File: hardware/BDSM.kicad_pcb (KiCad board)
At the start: 2 copper layers, 80 x 56 mm, 97 parts, among them J1 614105150721, Q1 BC847, Q2 BC847, Q3 BSS138, Q4 BSS138, Q5 BSS138, SW1 "ON/OFF", U1 MAX16054AZT+T, U2 BQ24070, U3 TPS63001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

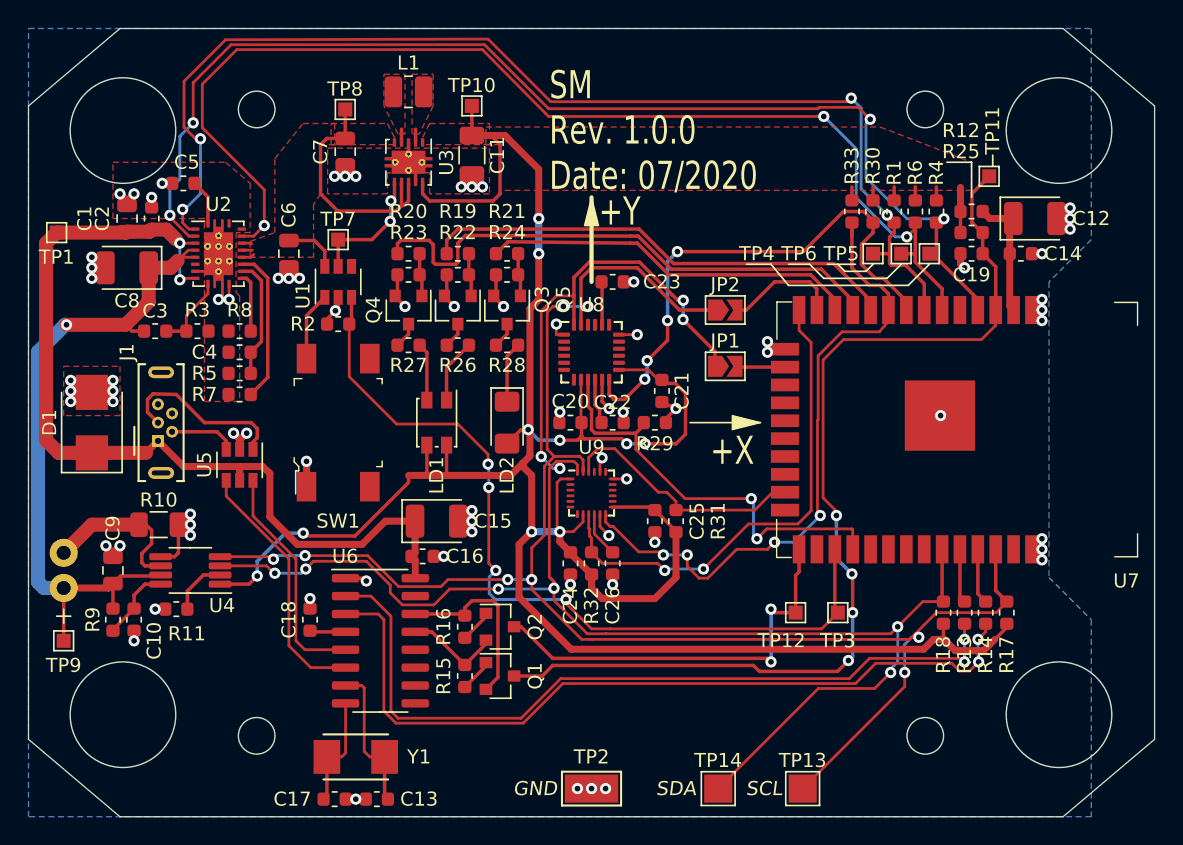
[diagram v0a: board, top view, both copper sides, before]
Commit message: Fix ESP32 powering errors
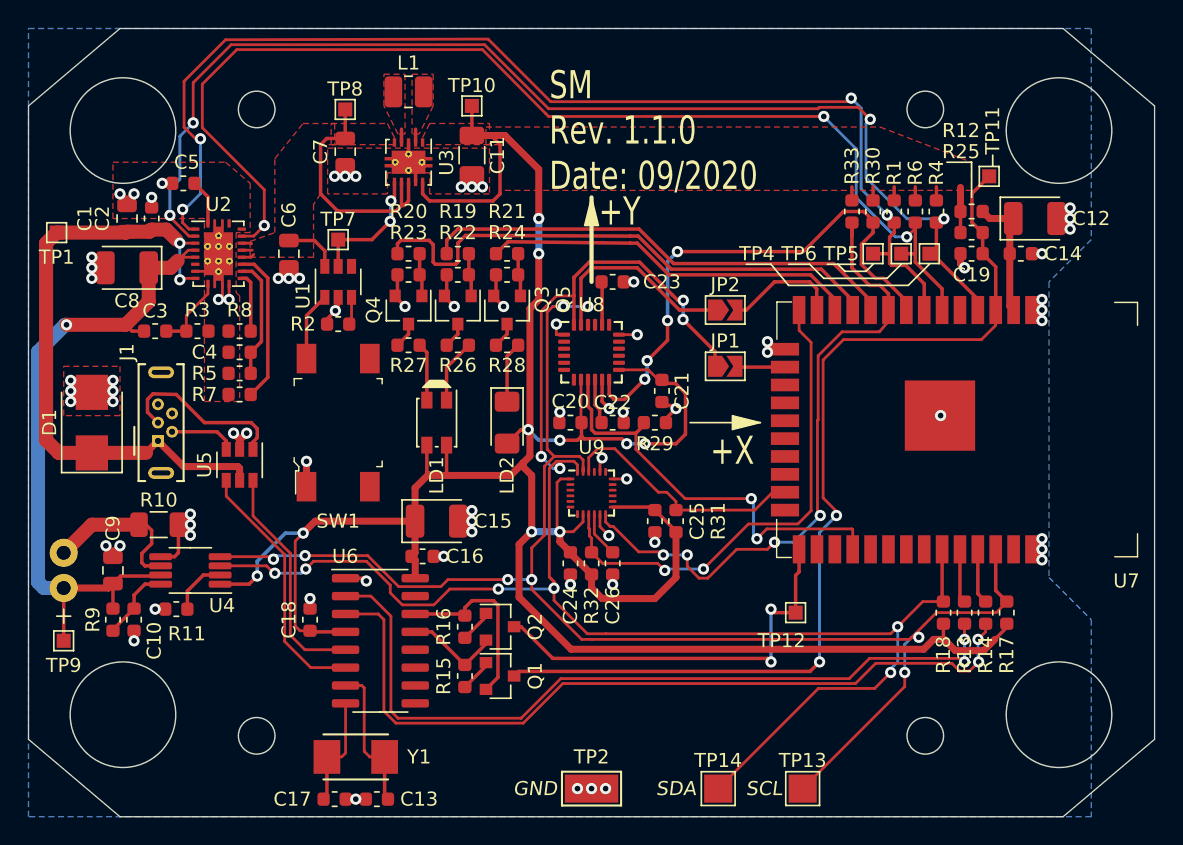
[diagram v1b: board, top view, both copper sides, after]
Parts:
- removed TP3: MCU-PWR, TestPoint:TestPoint_Pad_1.0x1.0mm
- Q1, Q2: value BC847 -> SS8050
- R32: value 10k -> DNP
- U9: value MPU-9250 -> DNP (MPU-9250 )
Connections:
- C15 pad 1: /ESP32/VBUS -> +3V3
- C16 pad 1: /ESP32/VBUS -> +3V3
- C18 pad 1: Net-(C18-Pad1) -> +3V3
- R2 pad 2: /ESP32/MCU-PWR-CNTRL -> Net-(R2-Pad2)
- U1 pad 3: /ESP32/MCU-PWR-CNTRL -> Net-(R2-Pad2)
- U6 pad 16: /ESP32/VBUS -> +3V3
- U6 pad 4: Net-(C18-Pad1) -> +3V3
- U7 pad 27: /ESP32/MCU-PWR-CNTRL -> Net-(U7-Pad27)
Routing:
- net /ESP32/MCU-PWR-CNTRL: track 59.2 -> 0.00 mm, vias 4 -> 0
- net /ESP32/VBUS: track 66.8 -> 45.3 mm
- net +3V3: track 185.2 -> 201.3 mm
- net Net-(C18-Pad1): track 2.56 -> 0.00 mm
- net /ESP32/nRST: track 72.0 -> 69.6 mm, vias 4 -> 2
- net Net-(R2-Pad2): track 0.00 -> 1.97 mm
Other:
- board text added: "SM Rev. 1.1.0 Date: 09/2020"
- board text removed: "SM Rev. 1.0.0 Date: 07/2020"
